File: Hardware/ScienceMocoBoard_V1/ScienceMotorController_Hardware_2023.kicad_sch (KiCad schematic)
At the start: 185 parts, among them J1 RJ45_LED_Shielded, J2 Conn_02x03_Counter_Clockwise, Q1 SI4156DY, Q10 SI4156DY, Q11 SI4156DY, Q12 SI4156DY, Q13 SI4156DY, Q14 SI4156DY, Q15 SI4156DY, Q16 SI4156DY, Q2 SI4156DY, Q3 SI4156DY, Q4 SI4156DY, Q5 SI4156DY, Q6 SI4156DY, Q7 SI4156DY, Q8 SI4156DY, Q9 SI4156DY, SW1 SW_Push, SW10 SW_Push, SW11 SW_DPDT_x2, SW2 SW_Push, SW3 SW_Push, SW4 SW_Push, SW5 SW_Push, SW6 SW_Push, SW7 SW_Push, SW8 SW_Push, SW9 SW_Push, U1 74LVC2G04, U10 IRS2005S, U11 Teensy4.1_DEV-16771, U12 74LVC2G04, U13 IRS2005S, U14 IRS2005S, U15 IRS2005S, U2 IRS2005S, U3 3V3 OKI, U4 TSR_1-2450, U5 74LVC2G04, U6 IRS2005S, U7 IRS2005S, U8 IRS2005S, U9 74LVC2G04

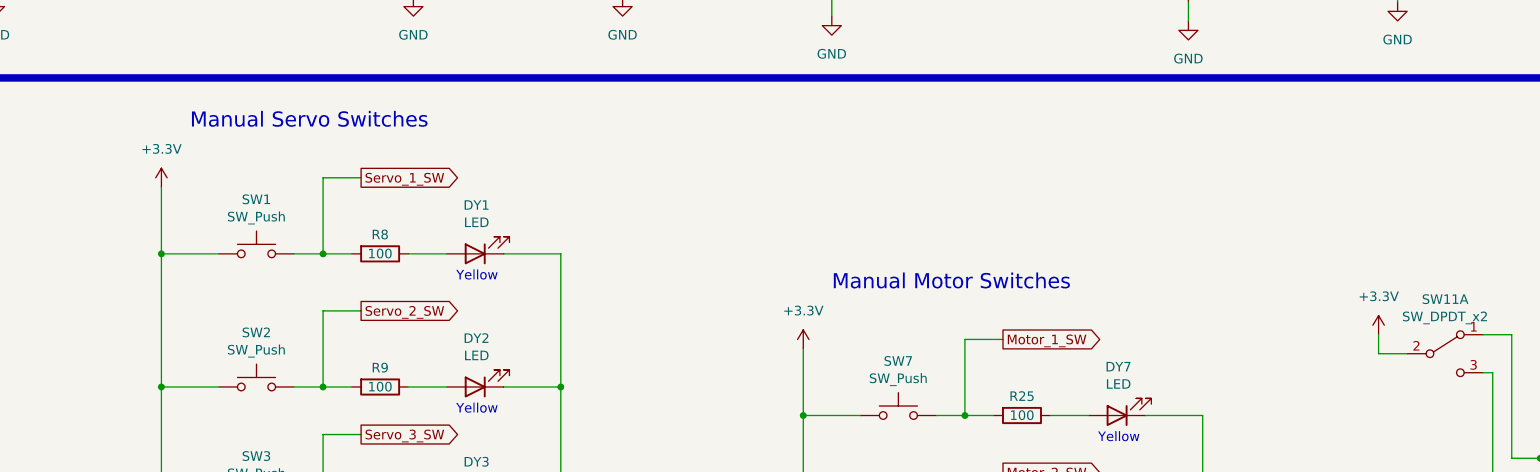
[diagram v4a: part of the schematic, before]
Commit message: Wired servo switches
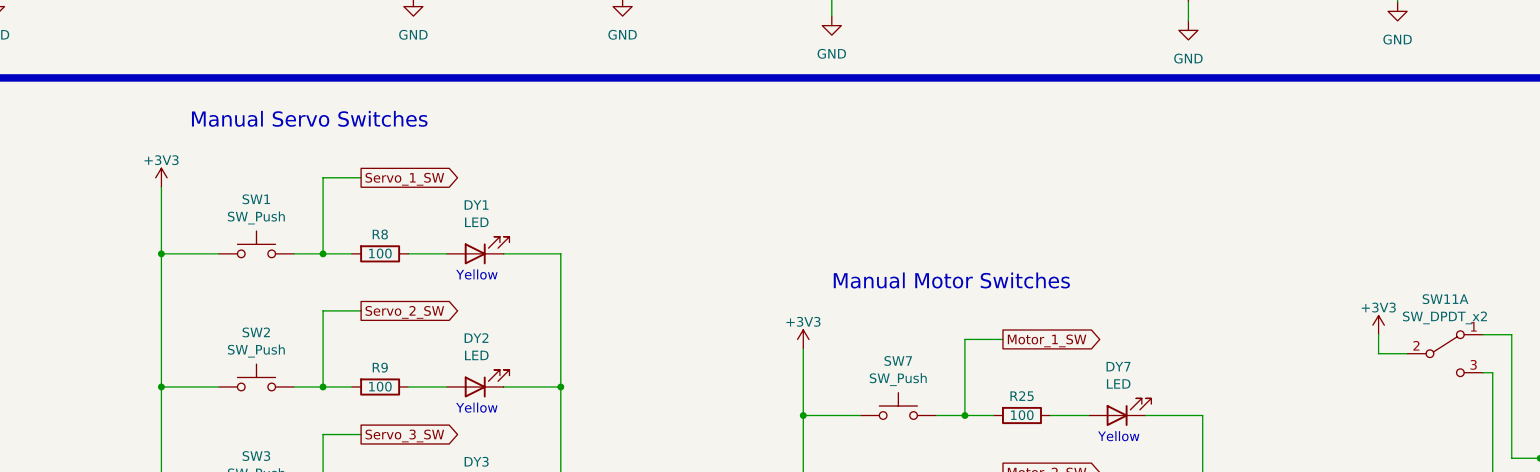
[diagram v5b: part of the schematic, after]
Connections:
- net +3.3V: no longer SW1.2, SW10.1, SW11.2 (B), SW2.1, SW3.1, SW4.1, SW5.1, SW6.1, SW7.2, SW8.1, SW9.1
- net +3V3: now also SW1.2, SW10.1, SW11.2 (B), SW2.1, SW3.1, SW4.1, SW5.1, SW6.1, SW7.2, SW8.1, SW9.1

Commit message: Finished buttons, servos, and encoders
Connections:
- net +3.3V is gone; now on net +3V3: U11.3.3V_1 (3.3V), U11.3.3V_2 (3.3V), U11.3.3V_3 (3.3V)
- net TX+: now reaches J1.1, J2.1 (Pin_1)
- net TX-: now reaches J1.3, J2.2 (Pin_2)
- net RX+: now reaches J1.4, J2.6 (Pin_6)
- net RX-: now reaches J1.6, J2.5 (Pin_5)
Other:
- note removed: "Rx +"
- note removed: "Rx -"
- note removed: "Tx +"
- note removed: "Tx -"

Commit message: Finished H Bridges
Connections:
- net FWD_PWM_1: now also U11.7 (RX2); no longer U11.0 (RX1)
- net FWD_PWM_2: now also U11.5 (IN2); no longer U11.2 (OUT2)
- net FWD_PWM_3: now also U11.3 (LRCLK2); no longer U11.4 (BCLK2)
- net FWD_PWM_4: now also U11.1 (TX1); no longer U11.6 (OUT1D)
- net RVS_PWM_1: now also U11.6 (OUT1D); no longer U11.1 (TX1)
- net RVS_PWM_2: now also U11.4 (BCLK2); no longer U11.3 (LRCLK2)
- net RVS_PWM_3: now also U11.2 (OUT2); no longer U11.5 (IN2)
- net RVS_PWM_4: now also U11.0 (RX1); no longer U11.7 (RX2)
- removed net 1M+: C10.1, C11.2, C13.1, C2.2, C3.1, C5.2, C7.1, C9.2, Conn4.1 (GND), Conn5.1 (GND), Conn6.1 (GND), Conn7.1 (GND), Q1.1 (S), Q1.2 (S), Q1.3 (S), Q10.5 (D), Q10.6 (D), Q10.7 (D), Q10.8 (D), Q11.1 (S), Q11.2 (S), Q11.3 (S), Q12.5 (D), Q12.6 (D), Q12.7 (D), Q12.8 (D), Q2.5 (D), Q2.6 (D), Q2.7 (D), Q2.8 (D), Q3.1 (S), Q3.2 (S), Q3.3 (S), Q4.5 (D), Q4.6 (D), Q4.7 (D), Q4.8 (D), Q9.1 (S), Q9.2 (S), Q9.3 (S), U10.6 (VS), U13.6 (VS), U2.6 (VS), U6.6 (VS)
- removed net 1M-: C10.2, C12.2, C13.2, C14.2, C3.2, C6.2, C7.2, C8.2, Conn4.2 (V+Log), Conn5.2 (V+Log), Conn6.2 (V+Log), Conn7.2 (V+Log), Q13.1 (S), Q13.2 (S), Q13.3 (S), Q14.5 (D), Q14.6 (D), Q14.7 (D), Q14.8 (D), Q15.1 (S), Q15.2 (S), Q15.3 (S), Q16.5 (D), Q16.6 (D), Q16.7 (D), Q16.8 (D), Q5.1 (S), Q5.2 (S), Q5.3 (S), Q6.5 (D), Q6.6 (D), Q6.7 (D), Q6.8 (D), Q7.1 (S), Q7.2 (S), Q7.3 (S), Q8.5 (D), Q8.6 (D), Q8.7 (D), Q8.8 (D), U14.6 (VS), U15.6 (VS), U7.6 (VS), U8.6 (VS)
- new net M1+: C5.2, C7.1, Conn5.1 (GND), Q3.1 (S), Q3.2 (S), Q3.3 (S), Q4.5 (D), Q4.6 (D), Q4.7 (D), Q4.8 (D), U6.6 (VS)
- new net M1-: C7.2, C8.2, Conn5.2 (V+Log), Q7.1 (S), Q7.2 (S), Q7.3 (S), Q8.5 (D), Q8.6 (D), Q8.7 (D), Q8.8 (D), U8.6 (VS)
- new net M2+: C11.2, C13.1, Conn7.1 (GND), Q11.1 (S), Q11.2 (S), Q11.3 (S), Q12.5 (D), Q12.6 (D), Q12.7 (D), Q12.8 (D), U13.6 (VS)
- new net M2-: C13.2, C14.2, Conn7.2 (V+Log), Q15.1 (S), Q15.2 (S), Q15.3 (S), Q16.5 (D), Q16.6 (D), Q16.7 (D), Q16.8 (D), U15.6 (VS)
- new net M3+: C10.1, C9.2, Conn6.1 (GND), Q10.5 (D), Q10.6 (D), Q10.7 (D), Q10.8 (D), Q9.1 (S), Q9.2 (S), Q9.3 (S), U10.6 (VS)
- new net M3-: C10.2, C12.2, Conn6.2 (V+Log), Q13.1 (S), Q13.2 (S), Q13.3 (S), Q14.5 (D), Q14.6 (D), Q14.7 (D), Q14.8 (D), U14.6 (VS)
- new net M4+: C2.2, C3.1, Conn4.1 (GND), Q1.1 (S), Q1.2 (S), Q1.3 (S), Q2.5 (D), Q2.6 (D), Q2.7 (D), Q2.8 (D), U2.6 (VS)
- new net M4-: C3.2, C6.2, Conn4.2 (V+Log), Q5.1 (S), Q5.2 (S), Q5.3 (S), Q6.5 (D), Q6.6 (D), Q6.7 (D), Q6.8 (D), U7.6 (VS)
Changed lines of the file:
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@@
     (effects (font (size 1.27 1.27)) (justify left bottom))
   )
-  (label "1M+" (at 101.6 109.22 0)
+  (label "M4+" (at 101.6 109.22 0)
     (effects (font (size 1.27 1.27)) (justify left bottom))
   )
@@
     (effects (font (size 1.27 1.27)) (justify left bottom))
   )
-  (label "1M+" (at 365.125 50.165 0)
-    (effects (font (size 1.27 1.27)) (justify left bottom))
-  )
-  (label "1M-" (at 146.05 109.22 0)
+  (label "M2+" (at 365.125 50.165 0)
+    (effects (font (size 1.27 1.27)) (justify left bottom))
+  )
+  (label "M4-" (at 146.05 109.22 0)
     (effects (font (size 1.27 1.27)) (justify left bottom))
   )
@@
     (effects (font (size 1.27 1.27)) (justify left bottom))
   )
-  (label "1M-" (at 198.755 48.895 0)
+  (label "M1-" (at 198.755 48.895 0)
     (effects (font (size 1.27 1.27)) (justify left bottom))
   )
@@
     (effects (font (size 1.27 1.27)) (justify left bottom))
   )
-  (label "1M+" (at 316.865 109.855 0)
-    (effects (font (size 1.27 1.27)) (justify left bottom))
-  )
-  (label "1M-" (at 409.575 50.165 0)
-    (effects (font (size 1.27 1.27)) (justify left bottom))
-  )
-  (label "1M-" (at 361.315 109.855 0)
-    (effects (font (size 1.27 1.27)) (justify left bottom))
-  )
-  (label "1M+" (at 154.305 48.895 0)
+  (label "M3+" (at 316.865 109.855 0)
+    (effects (font (size 1.27 1.27)) (justify left bottom))
+  )
+  (label "M2-" (at 409.575 50.165 0)
+    (effects (font (size 1.27 1.27)) (justify left bottom))
+  )
+  (label "M3-" (at 361.315 109.855 0)
+    (effects (font (size 1.27 1.27)) (justify left bottom))
+  )
+  (label "M1+" (at 154.305 48.895 0)
     (effects (font (size 1.27 1.27)) (justify left bottom))
   )
@@
     )
   )
-  (global_label "FWD_PWM_2" (shape output) (at 426.72 332.105 0) (fields_autoplaced)
-    (effects (font (size 1.27 1.27)) (justify left))
-    (property "Intersheet References" "${INTERSHEET_REFS}" (id 0) (at 440.2607 332.0256 0)
-      (effects (font (size 1.27 1.27)) (justify left) hide)
+  (global_label "FWD_PWM_2" (shape output) (at 377.825 311.785 180) (fields_autoplaced)
+    (effects (font (size 1.27 1.27)) (justify right))
+    (property "Intersheet References" "${INTERSHEET_REFS}" (id 0) (at 364.2843 311.8644 0)
+      (effects (font (size 1.27 1.27)) (justify right) hide)
     )
   )
@@
     )
   )
-  (global_label "RVS_PWM_1" (shape output) (at 377.825 327.025 180) (fields_autoplaced)
-    (effects (font (size 1.27 1.27)) (justify right))
-    (property "Intersheet References" "${INTERSHEET_REFS}" (id 0) (at 364.5262 327.1044 0)
-      (effects (font (size 1.27 1.27)) (justify right) hide)
+  (global_label "RVS_PWM_1" (shape output) (at 426.72 334.645 0) (fields_autoplaced)
+    (effects (font (size 1.27 1.27)) (justify left))
+    (property "Intersheet References" "${INTERSHEET_REFS}" (id 0) (at 440.0188 334.5656 0)
+      (effects (font (size 1.27 1.27)) (justify left) hide)
     )
   )
@@
     )
   )
-  (global_label "FWD_PWM_3" (shape output) (at 377.825 354.965 180) (fields_autoplaced)
-    (effects (font (size 1.27 1.27)) (justify right))
-    (property "Intersheet References" "${INTERSHEET_REFS}" (id 0) (at 364.2843 355.0444 0)
+  (global_label "FWD_PWM_3" (shape output) (at 377.825 352.425 180) (fields_autoplaced)
+    (effects (font (size 1.27 1.27)) (justify right))
+    (property "Intersheet References" "${INTERSHEET_REFS}" (id 0) (at 364.2843 352.5044 0)
       (effects (font (size 1.27 1.27)) (justify right) hide)
     )
@@
     )
   )
-  (global_label "RVS_PWM_2" (shape output) (at 377.825 352.425 180) (fields_autoplaced)
-    (effects (font (size 1.27 1.27)) (justify right))
-    (property "Intersheet References" "${INTERSHEET_REFS}" (id 0) (at 364.5262 352.5044 0)
+  (global_label "RVS_PWM_2" (shape output) (at 377.825 354.965 180) (fields_autoplaced)
+    (effects (font (size 1.27 1.27)) (justify right))
+    (property "Intersheet References" "${INTERSHEET_REFS}" (id 0) (at 364.5262 355.0444 0)
       (effects (font (size 1.27 1.27)) (justify right) hide)
     )
@@
     )
   )
-  (global_label "RVS_PWM_4" (shape output) (at 377.825 329.565 180) (fields_autoplaced)
-    (effects (font (size 1.27 1.27)) (justify right))
-    (property "Intersheet References" "${INTERSHEET_REFS}" (id 0) (at 364.5262 329.6444 0)
+  (global_label "RVS_PWM_4" (shape output) (at 377.825 324.485 180) (fields_autoplaced)
+    (effects (font (size 1.27 1.27)) (justify right))
+    (property "Intersheet References" "${INTERSHEET_REFS}" (id 0) (at 364.5262 324.5644 0)
       (effects (font (size 1.27 1.27)) (justify right) hide)
     )
@@
     )
   )
-  (global_label "FWD_PWM_1" (shape output) (at 377.825 324.485 180) (fields_autoplaced)
-    (effects (font (size 1.27 1.27)) (justify right))
-    (property "Intersheet References" "${INTERSHEET_REFS}" (id 0) (at 364.2843 324.5644 0)
-      (effects (font (size 1.27 1.27)) (justify right) hide)
-    )
-  )
-  (global_label "FWD_PWM_4" (shape output) (at 426.72 334.645 0) (fields_autoplaced)
-    (effects (font (size 1.27 1.27)) (justify left))
-    (property "Intersheet References" "${INTERSHEET_REFS}" (id 0) (at 440.2607 334.5656 0)
-      (effects (font (size 1.27 1.27)) (justify left) hide)
+  (global_label "FWD_PWM_1" (shape output) (at 377.825 329.565 180) (fields_autoplaced)
+    (effects (font (size 1.27 1.27)) (justify right))
+    (property "Intersheet References" "${INTERSHEET_REFS}" (id 0) (at 364.2843 329.6444 0)
+      (effects (font (size 1.27 1.27)) (justify right) hide)
+    )
+  )
+  (global_label "FWD_PWM_4" (shape output) (at 377.825 327.025 180) (fields_autoplaced)
+    (effects (font (size 1.27 1.27)) (justify right))
+    (property "Intersheet References" "${INTERSHEET_REFS}" (id 0) (at 364.2843 327.1044 0)
+      (effects (font (size 1.27 1.27)) (justify right) hide)
     )
   )
@@
     )
   )
-  (global_label "RVS_PWM_3" (shape output) (at 377.825 311.785 180) (fields_autoplaced)
-    (effects (font (size 1.27 1.27)) (justify right))
-    (property "Intersheet References" "${INTERSHEET_REFS}" (id 0) (at 364.5262 311.8644 0)
-      (effects (font (size 1.27 1.27)) (justify right) hide)
-    )
-  )
+  (global_label "RVS_PWM_3" (shape output) (at 426.72 332.105 0) (fields_autoplaced)
+    (effects (font (size 1.27 1.27)) (justify left))
+    (property "Intersheet References" "${INTERSHEET_REFS}" (id 0) (at 440.0188 332.0256 0)
+      (effects (font (size 1.27 1.27)) (justify left) hide)
+    )
+  )

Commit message: Worked on traces
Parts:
- D1, D15, D16, D18, D21, D23, D4, D7: value Pink -> Orange
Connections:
- net Servo_4: now also U11.13 (SCK); no longer U11.11 (MOSI)
- net Servo_5_SW: now also U11.31 (CTX3); no longer U11.30 (CRX3)
- net Servo_6: now also U11.11 (MOSI); no longer U11.13 (SCK)
- net Servo_6_SW: now also U11.32 (OUT1B); no longer U11.31 (CTX3)
